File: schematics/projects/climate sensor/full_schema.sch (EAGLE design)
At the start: 47 parts, among them Q1 2N3906BU, Q2 2N3906BU, Q3 2N3906BU, Q4 2N3904, Q5 2N3904

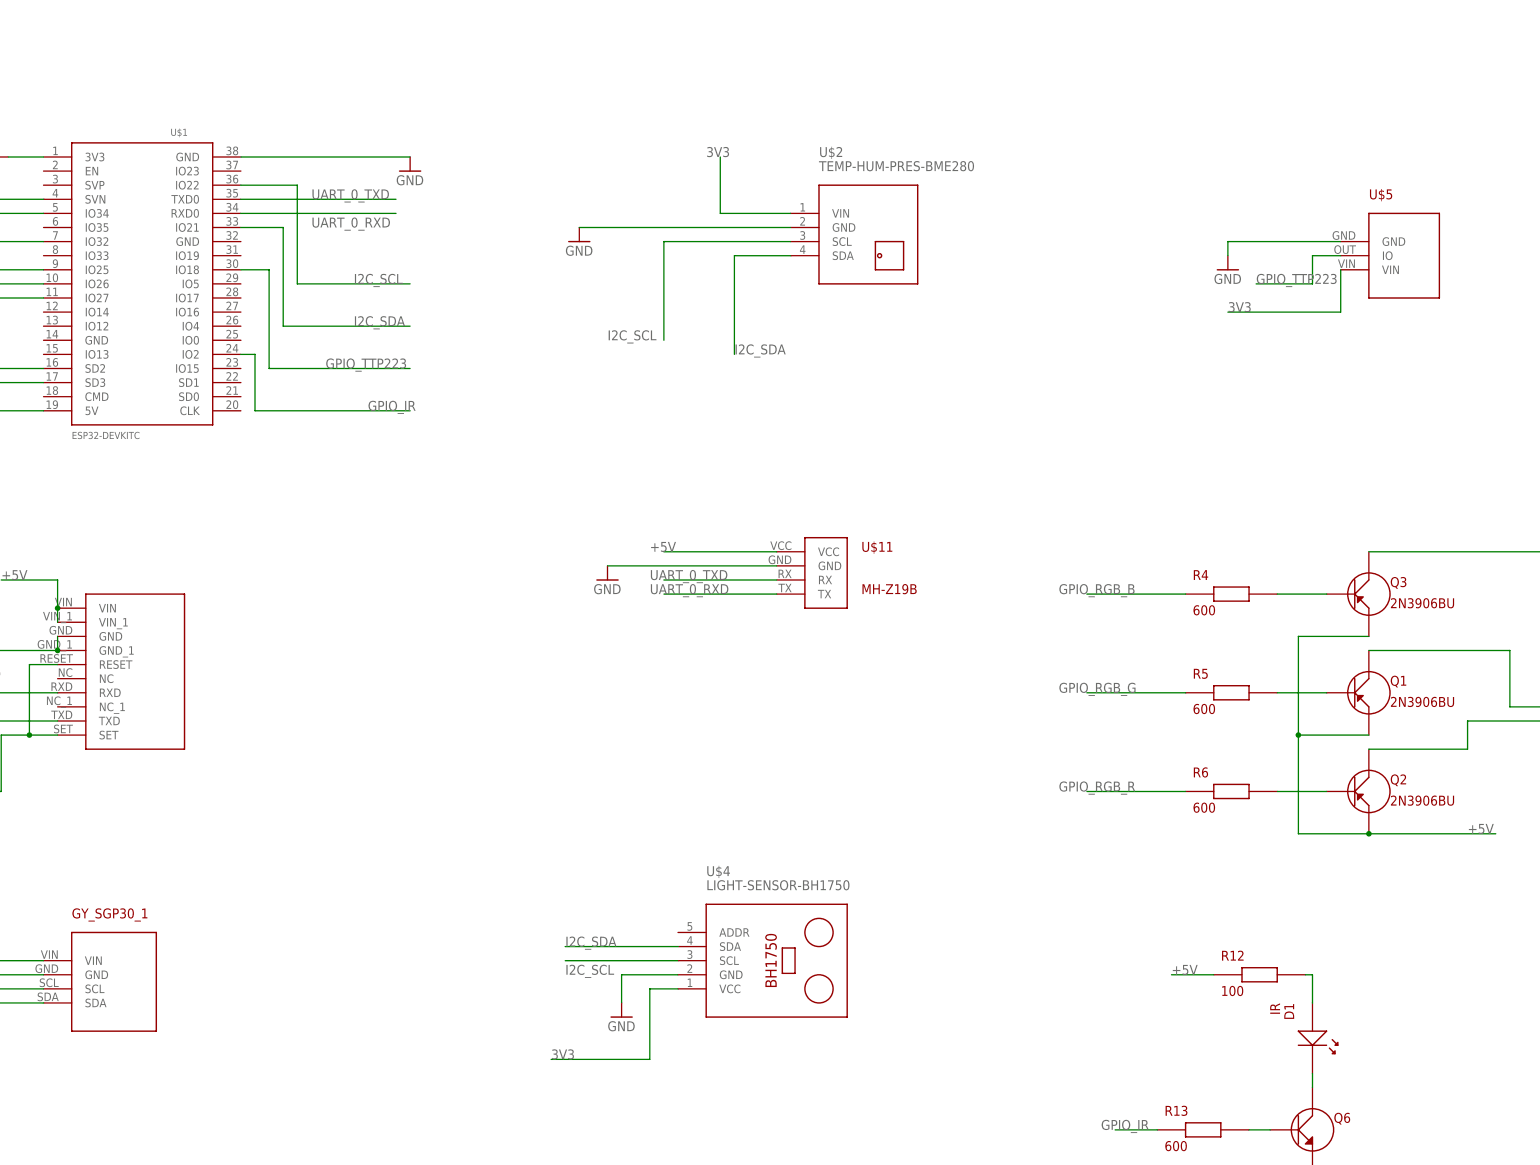
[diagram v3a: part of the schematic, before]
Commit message: added buildin touch sensor, maybe I will use it.
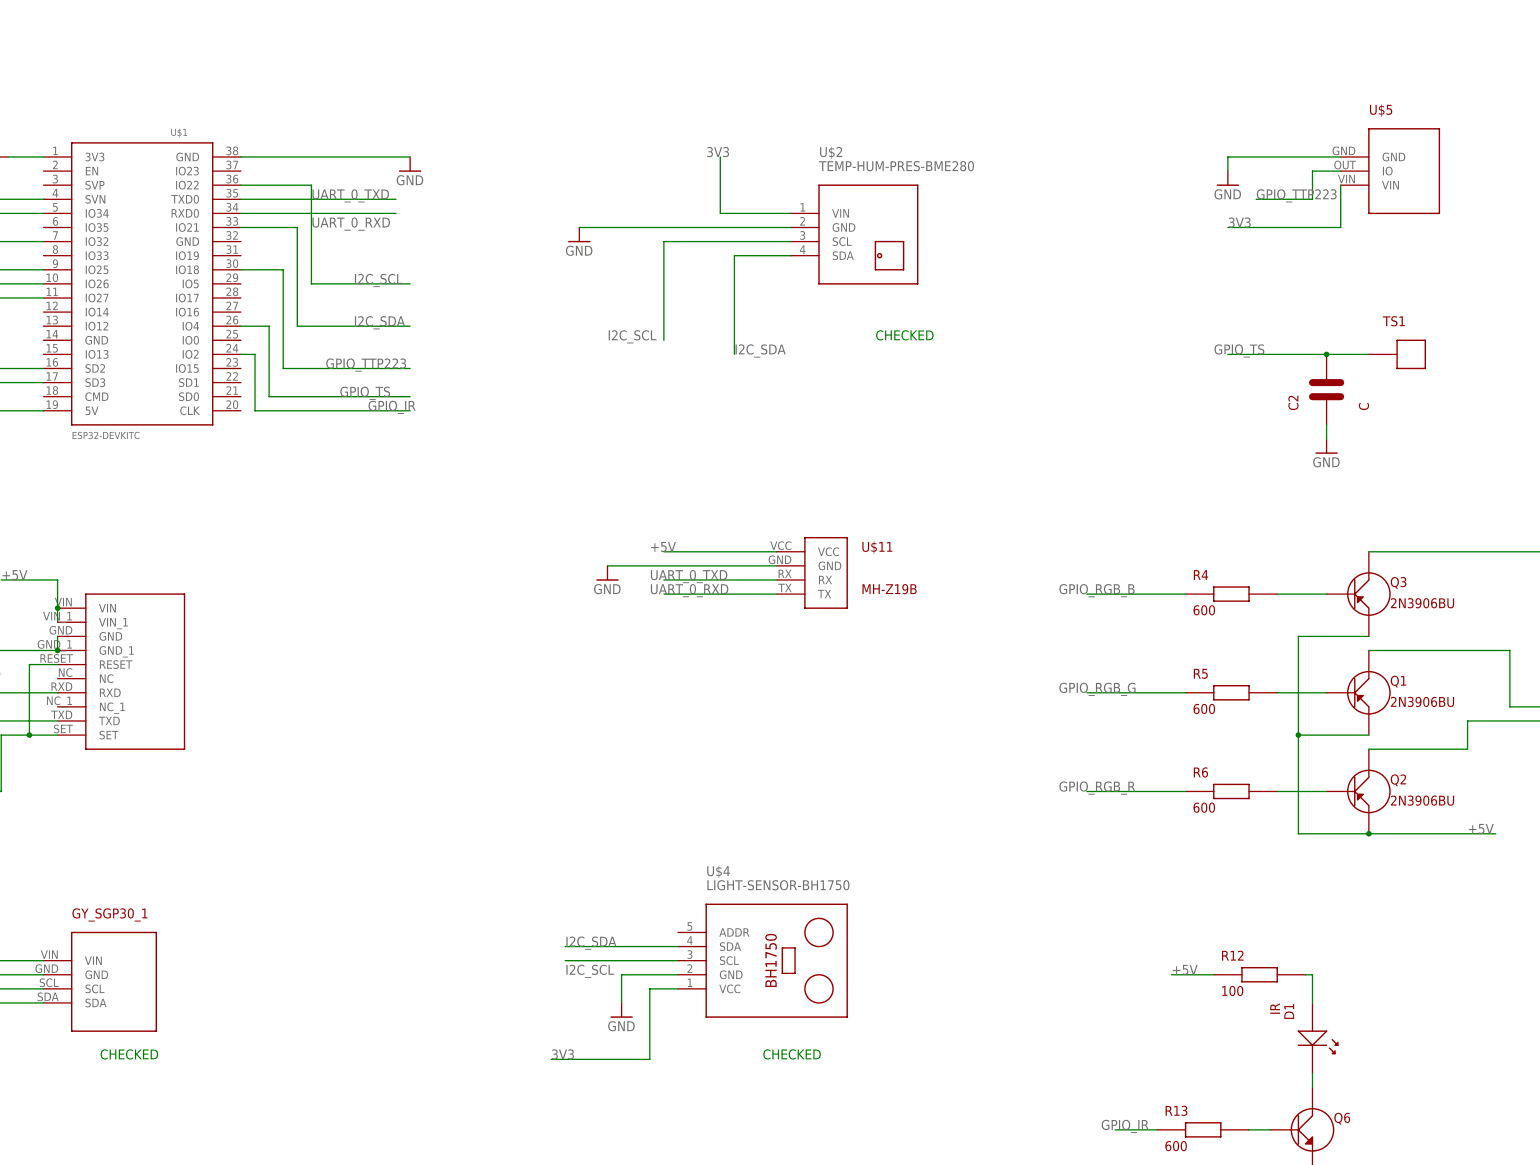
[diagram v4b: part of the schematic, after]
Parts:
- added C2: C, my_devices:C
- added TS1: TOUCH_SENSOR, my_devices:TOUCH_SENSOR
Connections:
- new net GPIO_TS: C2.P$2, TS1.P$1, U$1.IO4
- net GND: now also C2.P$1
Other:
- note added: "CHECKED"
- moved on the sheet: U$5
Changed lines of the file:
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@@
 <schematic_group name="FAN"/>
 <schematic_group name="IR"/>
+<schematic_group name="TOUCH_SENSOR"/>
 </groups>
 <parts>
@@
 <part name="R12" library="my_devices" deviceset="R" device="" value="100"/>
 <part name="R13" library="my_devices" deviceset="R" device="" value="600"/>
+<part name="TS1" library="my_devices" deviceset="TOUCH_SENSOR" device=""/>
+<part name="C2" library="my_devices" deviceset="C" device=""/>
+<part name="GND14" library="supply1" library_urn="urn:adsk.eagle:library:371" deviceset="GND" device=""/>
 </parts>
 <sheets>
@@
 <text x="-121.92" y="-50.8" size="1.778" layer="91">Low voltage block</text>
 <text x="-124.46" y="-76.2" size="1.778" layer="91" grouprefs="FAN">Cabel to FAN block and FAN block</text>
+<text x="-45.72" y="-58.42" size="1.778" layer="91">CHECKED</text>
+<text x="73.66" y="-58.42" size="1.778" layer="91">CHECKED</text>
+<text x="93.98" y="71.12" size="1.778" layer="91">CHECKED</text>
 </plain>
 <instances>
@@
 <attribute name="VALUE" x="-78.74" y="-50.8" size="1.778" layer="96"/>
 </instance>
-<instance part="GND7" gate="1" x="157.48" y="83.82" smashed="yes" grouprefs="TTP223">
-<attribute name="VALUE" x="154.94" y="81.28" size="1.778" layer="96"/>
+<instance part="GND7" gate="1" x="157.48" y="99.06" smashed="yes" grouprefs="TTP223">
+<attribute name="VALUE" x="154.94" y="96.52" size="1.778" layer="96"/>
 </instance>
 <instance part="GND8" gate="1" x="218.44" y="-2.54" smashed="yes" grouprefs="RGBLED">
@@
 <attribute name="NAME" x="-50.8" y="-33.02" size="1.778" layer="94"/>
 </instance>
-<instance part="U$5" gate="G$1" x="185.42" y="86.36" smashed="yes" grouprefs="TTP223">
-<attribute name="NAME" x="182.88" y="96.52" size="1.778" layer="94"/>
+<instance part="U$5" gate="G$1" x="185.42" y="101.6" smashed="yes" grouprefs="TTP223">
+<attribute name="NAME" x="182.88" y="111.76" size="1.778" layer="94"/>
 </instance>
 <instance part="U$6" gate="G$1" x="228.6" y="5.08" smashed="yes" grouprefs="RGBLED">
@@
 <attribute name="NAME" x="146.05" y="-68.58" size="1.778" layer="94"/>
 <attribute name="VALUE" x="146.05" y="-74.93" size="1.778" layer="94"/>
+</instance>
+<instance part="TS1" gate="G$1" x="190.5" y="68.58" smashed="yes" grouprefs="TOUCH_SENSOR">
+<attribute name="NAME" x="185.42" y="73.66" size="1.778" layer="94"/>
+</instance>
+<instance part="C2" gate="G$1" x="175.26" y="63.5" smashed="yes" rot="R90" grouprefs="TOUCH_SENSOR">
+<attribute name="NAME" x="170.18" y="58.42" size="1.778" layer="94" rot="R90"/>
+<attribute name="VALUE" x="182.88" y="58.42" size="1.778" layer="94" rot="R90"/>
+</instance>
+<instance part="GND14" gate="1" x="175.26" y="50.8" smashed="yes" grouprefs="TOUCH_SENSOR">
+<attribute name="VALUE" x="172.72" y="48.26" size="1.778" layer="96"/>
 </instance>
 </instances>
@@
 </segment>
 <segment>
-<wire x1="177.8" y1="88.9" x2="157.48" y2="88.9" width="0.1524" layer="91" grouprefs="TTP223"/>
-<wire x1="157.48" y1="88.9" x2="157.48" y2="86.36" width="0.1524" layer="91" grouprefs="TTP223"/>
+<wire x1="177.8" y1="104.14" x2="157.48" y2="104.14" width="0.1524" layer="91" grouprefs="TTP223"/>
+<wire x1="157.48" y1="104.14" x2="157.48" y2="101.6" width="0.1524" layer="91" grouprefs="TTP223"/>
 <pinref part="GND7" gate="1" pin="GND"/>
 <pinref part="U$5" gate="G$1" pin="GND"/>
@@
 <wire x1="172.72" y1="-78.74" x2="172.72" y2="-81.28" width="0.1524" layer="91" grouprefs="IR"/>
 </segment>
+<segment>
+<pinref part="C2" gate="G$1" pin="P$1"/>
+<pinref part="GND14" gate="1" pin="GND"/>
+<wire x1="175.26" y1="55.88" x2="175.26" y2="53.34" width="0.1524" layer="91" grouprefs="TOUCH_SENSOR"/>
+</segment>
 </net>
 <net name="I2C_SCL" class="0">
@@
 <segment>
 <pinref part="U$1" gate="G$1" pin="IO22"/>
-<wire x1="-20.32" y1="99.06" x2="-10.16" y2="99.06" width="0.1524" layer="91"/>
-<wire x1="-10.16" y1="99.06" x2="-10.16" y2="81.28" width="0.1524" layer="91" grouprefs="ESP"/>
-<wire x1="-10.16" y1="81.28" x2="10.16" y2="81.28" width="0.1524" layer="91" grouprefs="ESP"/>
+<wire x1="-20.32" y1="99.06" x2="-7.62" y2="99.06" width="0.1524" layer="91"/>
+<wire x1="-7.62" y1="99.06" x2="-7.62" y2="81.28" width="0.1524" layer="91" grouprefs="ESP"/>
+<wire x1="-7.62" y1="81.28" x2="10.16" y2="81.28" width="0.1524" layer="91" grouprefs="ESP"/>
 <label x="0" y="81.28" size="1.778" layer="95" grouprefs="ESP"/>
 </segment>
@@
 <segment>
 <pinref part="U$1" gate="G$1" pin="IO21"/>
-<wire x1="-20.32" y1="91.44" x2="-12.7" y2="91.44" width="0.1524" layer="91"/>
-<wire x1="-12.7" y1="91.44" x2="-12.7" y2="73.66" width="0.1524" layer="91" grouprefs="ESP"/>
-<wire x1="-12.7" y1="73.66" x2="10.16" y2="73.66" width="0.1524" layer="91" grouprefs="ESP"/>
+<wire x1="-20.32" y1="91.44" x2="-10.16" y2="91.44" width="0.1524" layer="91"/>
+<wire x1="-10.16" y1="91.44" x2="-10.16" y2="73.66" width="0.1524" layer="91" grouprefs="ESP"/>
+<wire x1="-10.16" y1="73.66" x2="10.16" y2="73.66" width="0.1524" layer="91" grouprefs="ESP"/>
 <label x="0" y="73.66" size="1.778" layer="95" grouprefs="ESP"/>
 </segment>
@@
 </segment>
 <segment>
-<wire x1="177.8" y1="83.82" x2="177.8" y2="76.2" width="0.1524" layer="91" grouprefs="TTP223"/>
-<wire x1="177.8" y1="76.2" x2="157.48" y2="76.2" width="0.1524" layer="91" grouprefs="TTP223"/>
-<label x="157.48" y="76.2" size="1.778" layer="95" grouprefs="TTP223"/>
+<wire x1="177.8" y1="99.06" x2="177.8" y2="91.44" width="0.1524" layer="91" grouprefs="TTP223"/>
+<wire x1="177.8" y1="91.44" x2="157.48" y2="91.44" width="0.1524" layer="91" grouprefs="TTP223"/>
+<label x="157.48" y="91.44" size="1.778" layer="95" grouprefs="TTP223"/>
 <pinref part="U$5" gate="G$1" pin="VIN"/>
 </segment>
@@
 <net name="GPIO_TTP223" class="0">
 <segment>
-<wire x1="177.8" y1="86.36" x2="172.72" y2="86.36" width="0.1524" layer="91" grouprefs="TTP223"/>
-<wire x1="172.72" y1="86.36" x2="172.72" y2="81.28" width="0.1524" layer="91" grouprefs="TTP223"/>
-<wire x1="172.72" y1="81.28" x2="162.56" y2="81.28" width="0.1524" layer="91" grouprefs="TTP223"/>
-<label x="162.56" y="81.28" size="1.778" layer="95" grouprefs="TTP223"/>
+<wire x1="177.8" y1="101.6" x2="172.72" y2="101.6" width="0.1524" layer="91" grouprefs="TTP223"/>
+<wire x1="172.72" y1="101.6" x2="172.72" y2="96.52" width="0.1524" layer="91" grouprefs="TTP223"/>
+<wire x1="172.72" y1="96.52" x2="162.56" y2="96.52" width="0.1524" layer="91" grouprefs="TTP223"/>
+<label x="162.56" y="96.52" size="1.778" layer="95" grouprefs="TTP223"/>
 <pinref part="U$5" gate="G$1" pin="IO"/>
 </segment>
 <segment>
 <pinref part="U$1" gate="G$1" pin="IO18"/>
-<wire x1="-20.32" y1="83.82" x2="-15.24" y2="83.82" width="0.1524" layer="91" grouprefs="ESP"/>
-<wire x1="-15.24" y1="83.82" x2="-15.24" y2="66.04" width="0.1524" layer="91" grouprefs="ESP"/>
-<wire x1="-15.24" y1="66.04" x2="10.16" y2="66.04" width="0.1524" layer="91" grouprefs="ESP"/>
+<wire x1="-20.32" y1="83.82" x2="-12.7" y2="83.82" width="0.1524" layer="91" grouprefs="ESP"/>
+<wire x1="-12.7" y1="83.82" x2="-12.7" y2="66.04" width="0.1524" layer="91" grouprefs="ESP"/>
+<wire x1="-12.7" y1="66.04" x2="10.16" y2="66.04" width="0.1524" layer="91" grouprefs="ESP"/>
 <label x="-5.08" y="66.04" size="1.778" layer="95" grouprefs="ESP"/>
 </segment>
@@
 </segment>
 </net>
+<net name="GPIO_TS" class="0">
+<segment>
+<pinref part="TS1" gate="G$1" pin="P$1"/>
+<pinref part="C2" gate="G$1" pin="P$2"/>
+<wire x1="182.88" y1="68.58" x2="175.26" y2="68.58" width="0.1524" layer="91" grouprefs="TOUCH_SENSOR"/>
+<wire x1="175.26" y1="68.58" x2="157.48" y2="68.58" width="0.1524" layer="91" grouprefs="TOUCH_SENSOR"/>
+<junction x="175.26" y="68.58" grouprefs="TOUCH_SENSOR"/>
+<label x="154.94" y="68.58" size="1.778" layer="95" grouprefs="TOUCH_SENSOR"/>
+</segment>
+<segment>
+<pinref part="U$1" gate="G$1" pin="IO4"/>
+<wire x1="-20.32" y1="73.66" x2="-15.24" y2="73.66" width="0.1524" layer="91"/>
+<wire x1="-15.24" y1="73.66" x2="-15.24" y2="60.96" width="0.1524" layer="91"/>
+<wire x1="-15.24" y1="60.96" x2="10.16" y2="60.96" width="0.1524" layer="91"/>
+<label x="-2.54" y="60.96" size="1.778" layer="95"/>
+</segment>
+</net>
